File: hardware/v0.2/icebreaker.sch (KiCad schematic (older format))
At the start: 41 parts, among them J14 Jumper, J15 Jumper, J16 Jumper, J17 Jumper, J18 Jumper, J19 Jumper, U2 3.3V, U3 1V2, U5 W25Q, U6 ICE5LP4K-SG48

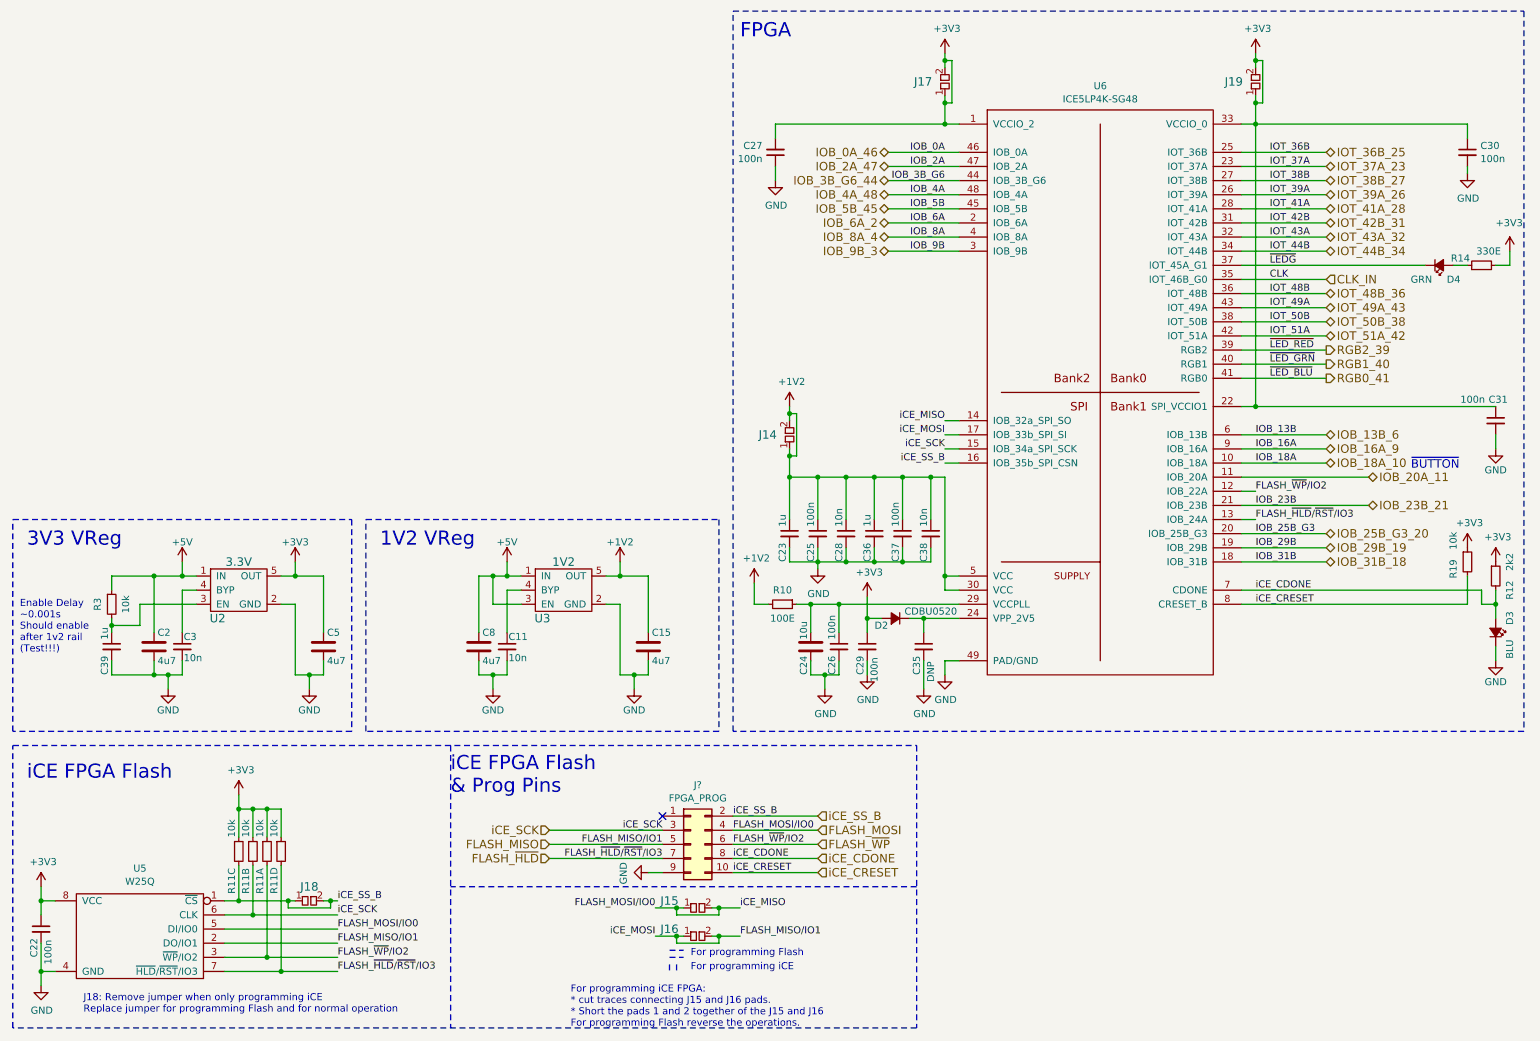
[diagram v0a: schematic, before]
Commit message: Added MEMS microphone input.
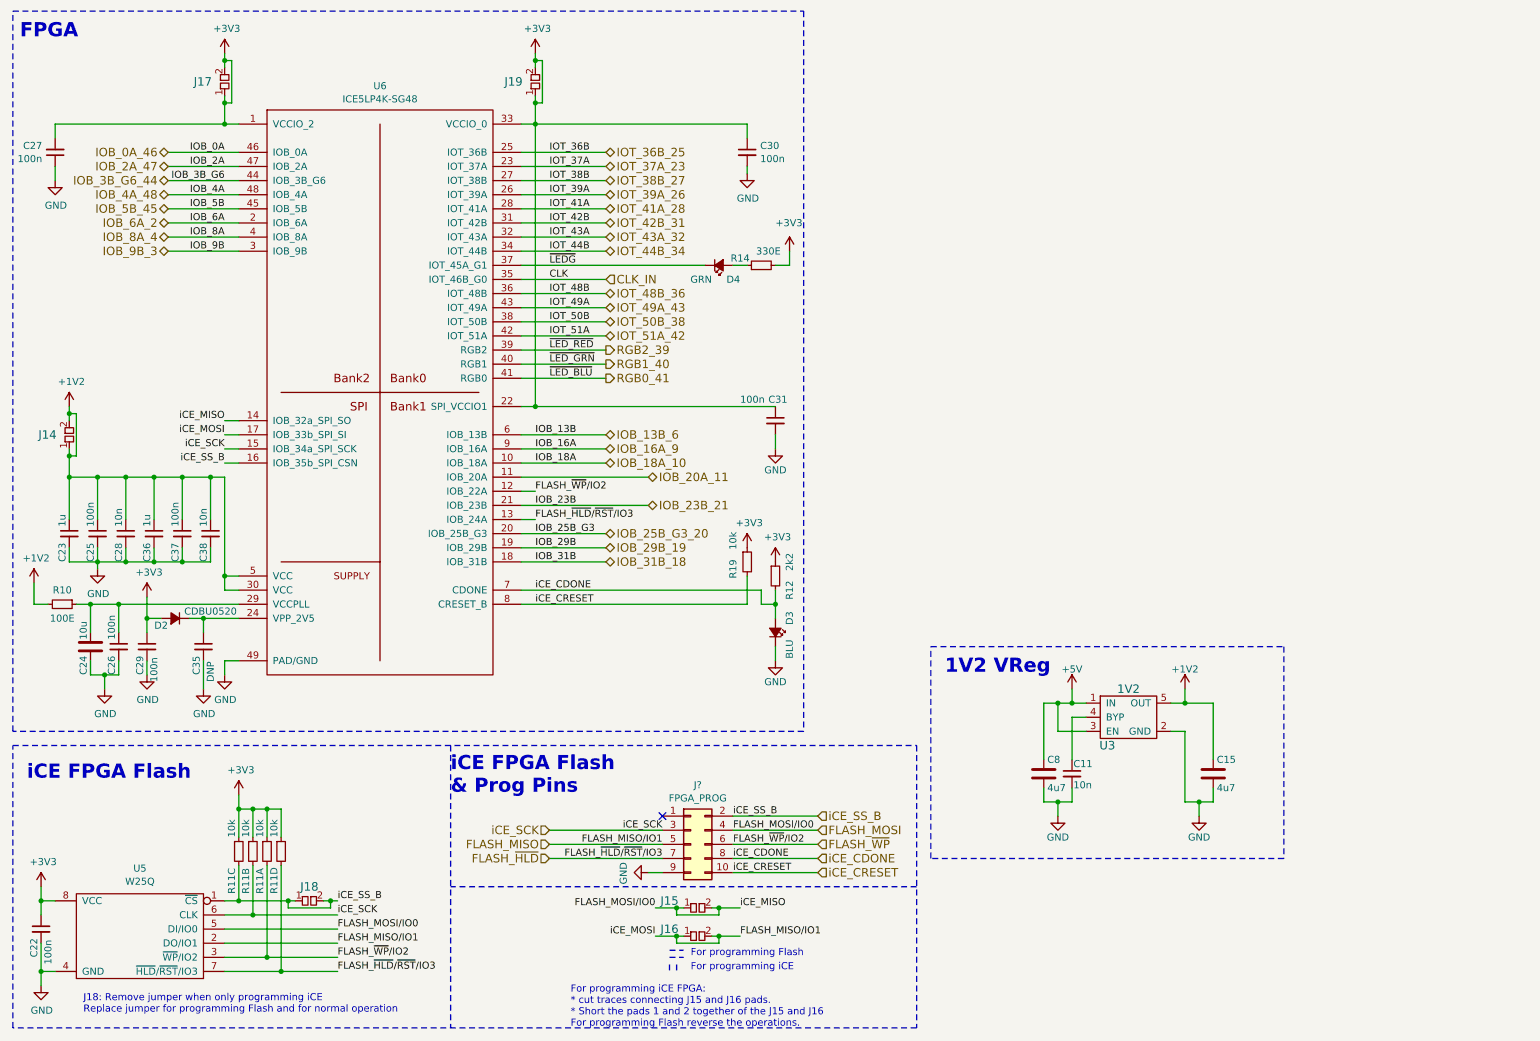
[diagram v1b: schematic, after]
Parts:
- removed C2, C5: 4u7, pkl_dipol:C_0603, symbol pkl_device:pkl_C
- removed C3: 10n, pkl_dipol:C_0402, symbol pkl_device:pkl_C_Small
- removed C39: 1u, pkl_dipol:C_0402, symbol pkl_device:pkl_C_Small
- removed R3: 10k, pkl_dipol:R_0402, symbol pkl_device:pkl_R_Small
- removed U2: 3.3V, pkl_housings_sot:SOT-23-5, symbol pkl_device:pkl_VREG_5PIN_FIXED
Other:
- note removed: "3V3 VReg"
- note removed: "Enable Delay\n~~0.001s\nShould enable\nafter 1v2 rail\n(Test!!!)"
- note removed: "~BUTTON"
- moved on the sheet: C11, C15, C23, C24, C25, C26, C27, C28, C29, C30, C31, C35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
